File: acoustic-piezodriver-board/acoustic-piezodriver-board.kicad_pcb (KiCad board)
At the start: 4 copper layers, 100 x 62 mm, 161 parts, among them J301 Conn_02x06_Odd_Even, J501 Conn_02x06_Odd_Even, P101 WJ128V-5.0-3P, P201 WJ128V-5.0-3P, Q501 AO3400A, Q502 AO3400A, U10 NCE6005AS, U101 AMS1117-3.3, U102 TMCS1108A3UQDR, U201 UCC27282DR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

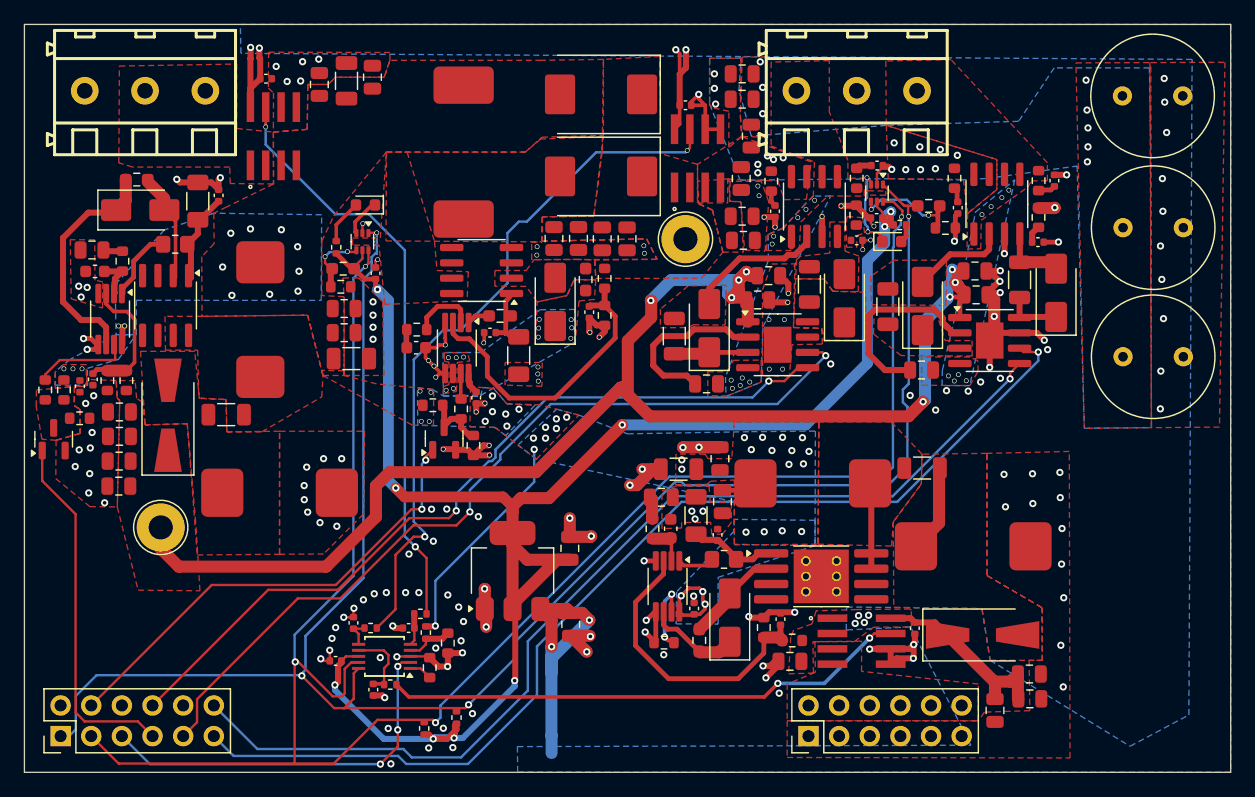
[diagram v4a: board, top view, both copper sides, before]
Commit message: checked components until mosfets
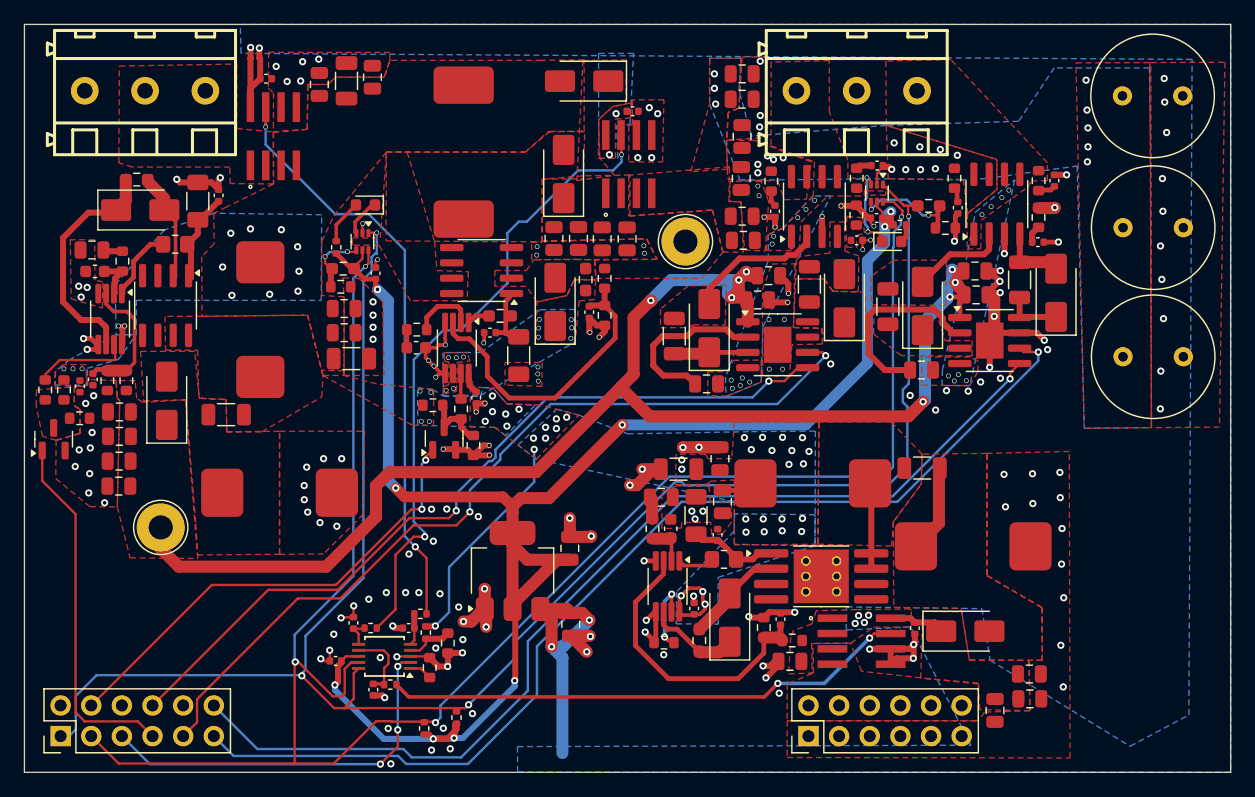
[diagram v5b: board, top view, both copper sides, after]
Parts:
- D2, D502: value SS52 -> SS54; footprint Diode_SMD:D_SMA-SMB_Universal_Handsoldering -> Diode_SMD:D_SMA
- D501, D504: footprint Diode_SMD:D_SMC -> Diode_SMD:D_SMA
- moved U204 5.72 mm to (94.1, 91.6)
- moved C210 4.41 mm to (94.4, 87.2)
- moved D504 3.11 mm to (88.7, 92.4), turned to 90 degrees
- moved D501 1.78 mm to (90.4, 84.7)
- moved D2 1.47 mm to (122.0, 130.3)
- moved D502 1.20 mm to (55.8, 111.2)
- moved C208 0.77 mm to (103.5, 89.3)
- moved TP501 0.20 mm to (98.8, 98.0)
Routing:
- net +6V: track 64.6 -> 41.9 mm
- net /INVERTER/ADC_IINV: track 59.0 -> 52.9 mm
- net GND: track 130.0 -> 126.0 mm, vias 173 -> 174
- net /INVERTER/+10V: track 121.8 -> 120.7 mm
- net +BATT: vias 51 -> 55

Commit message: completed footprint check (next) reroute pbootstrap circuit on top layer only, fix errors after footprint change
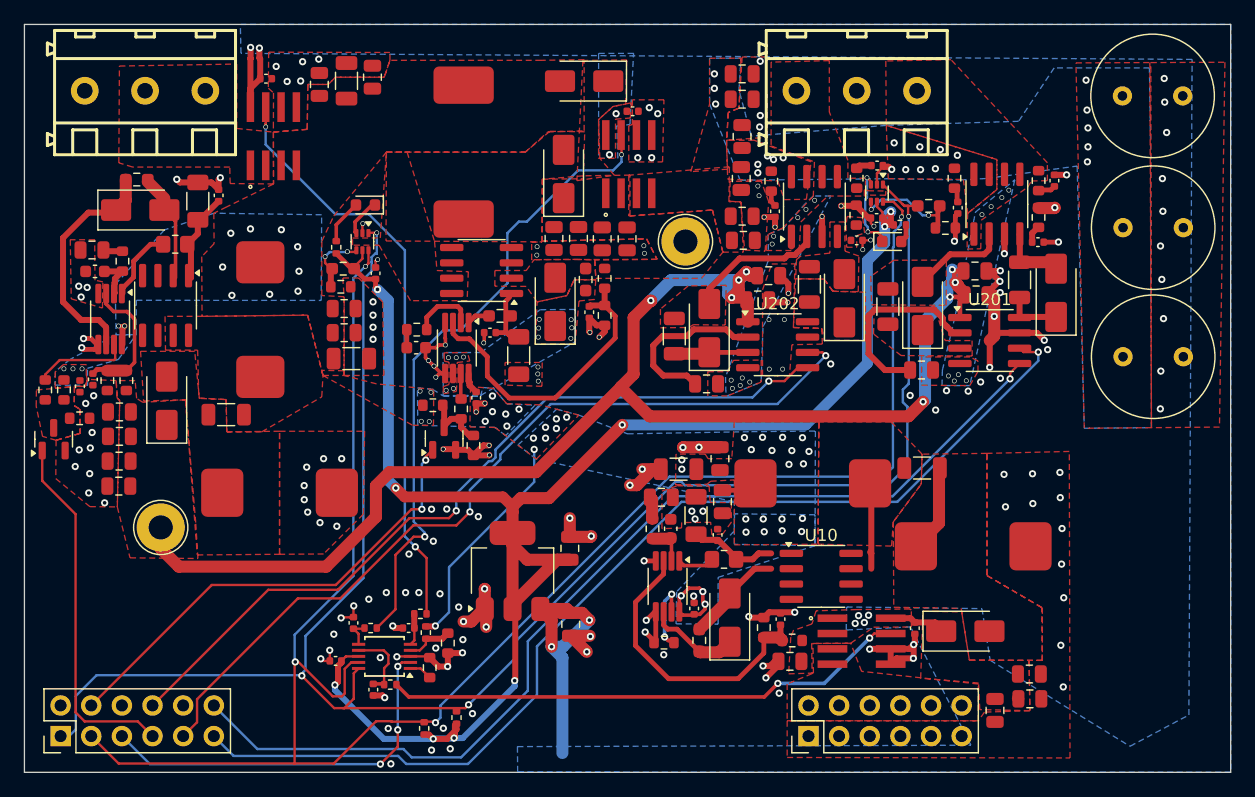
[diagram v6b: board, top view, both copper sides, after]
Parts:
- U10: footprint Package_SO:SOP-8-1EP_4.57x4.57mm_P1.27mm_EP4.57x4.45mm_ThermalVias -> Package_SO:SOIC-8_3.9x4.9mm_P1.27mm
- U201, U202: footprint Package_SO:SOIC-8-1EP_3.9x4.9mm_P1.27mm_EP2.29x3mm -> Package_SO:SOIC-8_3.9x4.9mm_P1.27mm
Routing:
- net GND: track 126.0 -> 126.5 mm

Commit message: Modified feedback path for low-impedance signals tobe closer to FB pin
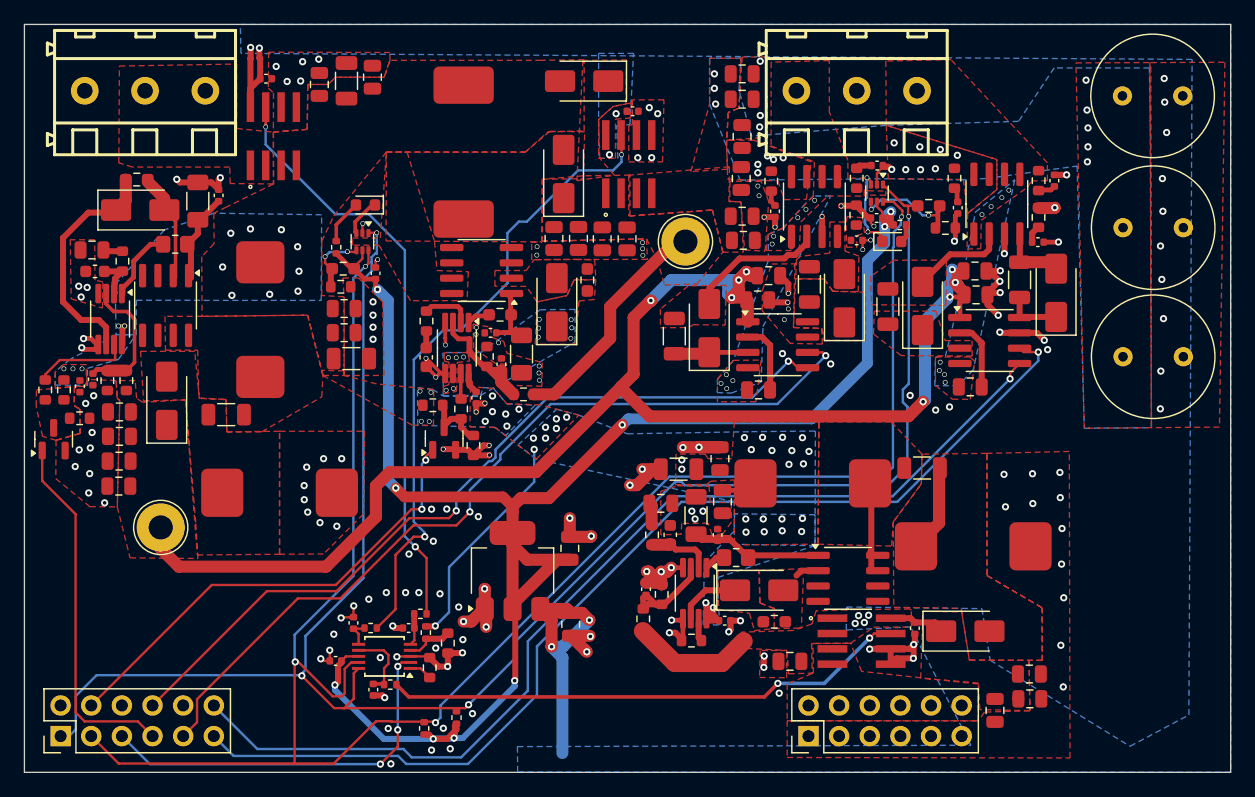
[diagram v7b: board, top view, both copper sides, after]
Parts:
- moved R23 12.5 mm to (95.3, 129.3), turned to 90 degrees
- moved R512 11.7 mm to (85.4, 110.7), turned to 180 degrees
- moved C39 11.4 mm to (95.5, 126.8)
- moved R518 10.3 mm to (82.3, 107.5), turned to 90 degrees
- moved R24 8.90 mm to (96.8, 127.2)
- moved C522 8.47 mm to (83.5, 108.2), turned to 90 degrees
- moved R20 6.41 mm to (106.2, 129.5), turned to 0 degrees
- moved C1 4.34 mm to (104.9, 110.3), turned to 180 degrees
- moved C2 4.27 mm to (122.4, 110.0), turned to 180 degrees
- moved D5 3.33 mm to (104.9, 126.9), turned to 0 degrees
- moved C301 2.73 mm to (102.1, 129.4), turned to 0 degrees
- moved U9 2.32 mm to (99.6, 127.2)
- moved R18 2.29 mm to (99.3, 131.1)
- moved U10 2.22 mm to (112.3, 125.9)
- moved C520 1.16 mm to (77.3, 107.6), turned to -90 degrees
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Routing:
- net /INVERTER/VINV_P: track 0.00 -> 19.4 mm
- net Net-(U9-FB): track 24.9 -> 8.72 mm
- net Net-(U504-FB): track 25.4 -> 11.0 mm
- net GND: track 126.5 -> 115.2 mm, vias 174 -> 170
- net +6V: track 41.9 -> 52.3 mm
- net Net-(U201-HB): track 15.9 -> 6.36 mm
- net Net-(U10B-S2): track 7.37 -> 16.1 mm
- net Net-(U202-HB): track 14.4 -> 5.83 mm
- net Net-(D5-A): track 8.31 -> 1.96 mm
- net Net-(U9-FA/SD): track 6.24 -> 1.57 mm, vias 2 -> 0
- net +BATT: track 35.0 -> 32.3 mm, vias 55 -> 54
- net Net-(D5-K): track 7.88 -> 5.70 mm
- net Net-(U9-COMP): track 3.46 -> 5.41 mm
- net Net-(U504-COMP): track 5.41 -> 4.20 mm
- net Net-(U9-I_{SEN}): track 3.08 -> 2.15 mm
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- added copper zone on F.Cu, net Net-(D5-A)
- added copper zone on F.Cu, net Net-(D5-K)
